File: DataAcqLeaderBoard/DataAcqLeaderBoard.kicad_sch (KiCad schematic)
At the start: 30 parts, among them SW1 UP, SW2 UP, SW3 UP, U1 PA1616S_GPS, X1 DigiXBeeRX900Micro

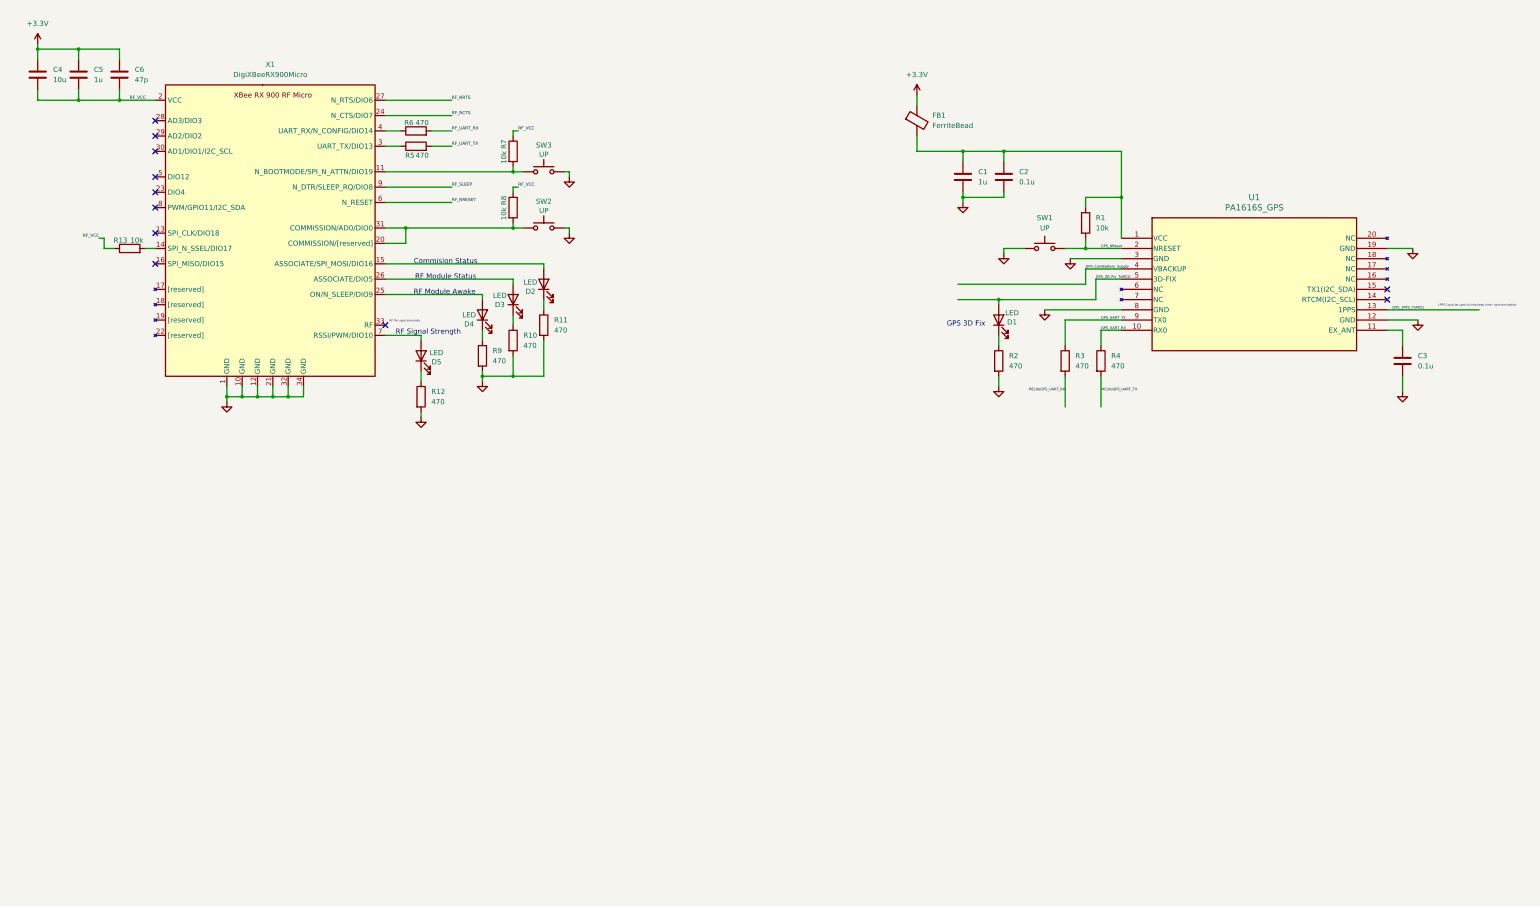
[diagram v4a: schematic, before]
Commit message: Added Digi XBee LTE Module
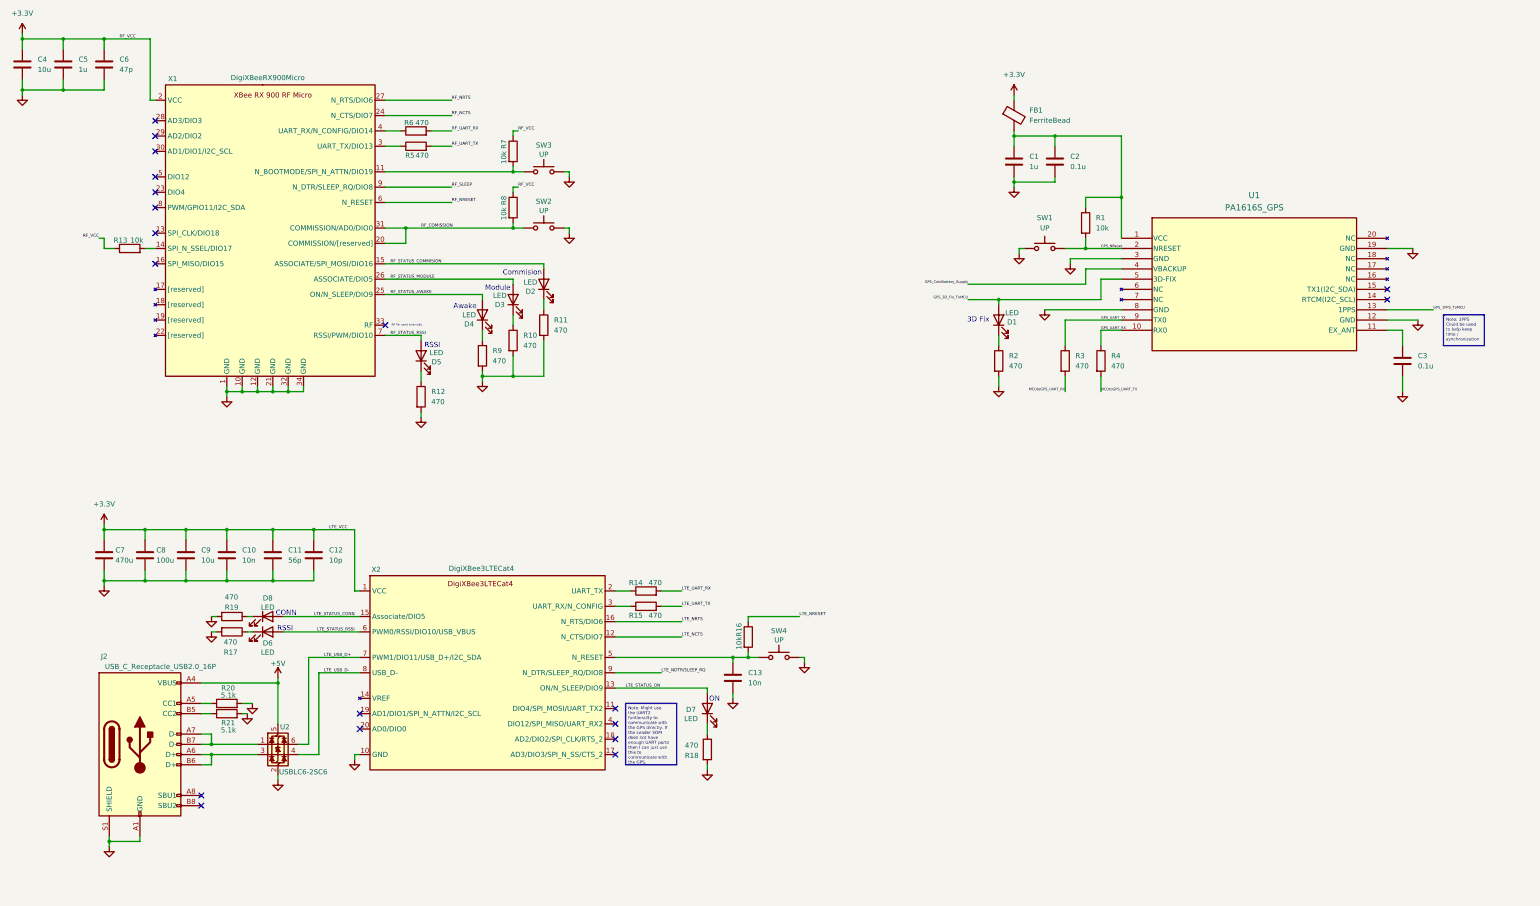
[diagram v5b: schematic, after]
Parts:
- added C10, C13: 10n, symbol Device:C
- added C11: 56p, symbol Device:C
- added C12: 10p, symbol Device:C
- added C7: 470u, symbol Device:C
- added C8: 100u, symbol Device:C
- added C9: 10u, symbol Device:C
- added D6, D7, D8: LED, symbol Device:LED
- added J2: USB_C_Receptacle_USB2.0_16P, symbol Connector:USB_C_Receptacle_USB2.0_16P
- added R14, R15, R17, R18, R19: 470, symbol Device:R
- added R16: 10k, symbol Device:R
- added R20, R21: 5.1k, symbol Device:R
- added SW4: UP, symbol Switch:SW_Push
- added U2: USBLC6-2SC6, Package_TO_SOT_SMD:SOT-23-6, symbol Power_Protection:USBLC6-2SC6
- added X2: DigiXBee3LTECat4, symbol DataAcqLeaderBoard-Symbols:DigiXBee3LTECat4
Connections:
- net +3.3V: now also R13.1, R7.1, R8.1, X1.2 (VCC), C10.1, C11.1, C12.1, C7.1, C8.1, C9.1, X2.1 (VCC)
- net GND: now also C4.2, C5.2, C6.2, C10.2, C11.2, C12.2, C13.2, C7.2, C8.2, C9.2, J2.A1 (GND), J2.A12 (GND), J2.B1 (GND), J2.B12 (GND), J2.S1 (SHIELD), R17.2, R18.2, R19.2, R20.2, R21.2, SW4.2, U2.2 (GND), X2.10 (GND)
- net RF_COMISSION: now reaches R8.2, SW2.1, X1.20 (COMMISSION/[reserved]), X1.31 (COMMISSION/AD0/DIO0)
- net RF_STATUS_MODULE: now reaches D3.2 (A), X1.26 (ASSOCIATE/DIO5)
- net RF_STATUS_COMMISION: now reaches D2.2 (A), X1.15 (ASSOCIATE/SPI_MOSI/DIO16)
- net RF_STATUS_AWAKE: now reaches D4.2 (A), X1.25 (ON/N_SLEEP/DIO9)
- net RF_STATUS_RSSI: now reaches D5.2 (A), X1.7 (RSSI/PWM/DIO10)
- removed net RF_VCC: C4.2, C5.2, C6.2, R13.1, R7.1, R8.1, X1.2 (VCC)
- new net: D7.1 (K), R18.1
- new net: R14.1, X2.2 (UART_TX)
- new net: C13.1, R16.2, SW4.1, X2.5 (N_RESET)
- new net: J2.A5 (CC1), R20.1
- new net: J2.A6 (D+), J2.B6 (D+), U2.3 (I/O2)
- new net: J2.A7 (D-), J2.B7 (D-), U2.1 (I/O1)
- new net: J2.B5 (CC2), R21.1
- new net: D6.1 (K), R17.1
- new net: D8.1 (K), R19.1
- new net: R15.1, X2.3 (UART_RX/N_CONFIG)
- new net +5V: J2.A4 (VBUS), J2.A9 (VBUS), J2.B4 (VBUS), J2.B9 (VBUS), U2.5 (VBUS)
- new net LTE_NCTS: X2.12 (N_CTS/DIO7)
- new net LTE_NDTR/SLEEP_RQ: X2.9 (N_DTR/SLEEP_RQ/DIO8)
- new net LTE_NRESET: R16.1
- new net LTE_NRTS: X2.16 (N_RTS/DIO6)
- new net LTE_STATUS_CONN: D8.2 (A), X2.15 (Associate/DIO5)
- new net LTE_STATUS_ON: D7.2 (A), X2.13 (ON/N_SLEEP/DIO9)
- new net LTE_STATUS_RSSI: D6.2 (A), X2.6 (PWM0/RSSI/DIO10/USB_VBUS)
- new net LTE_UART_RX: R14.2
- new net LTE_UART_TX: R15.2
- new net LTE_USB_D+: U2.6 (I/O1), X2.7 (PWM1/DIO11/USB_D+/I2C_SDA)
- new net LTE_USB_D-: U2.4 (I/O2), X2.8 (USB_D-)
- no-connect marks 11 -> 19
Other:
- note added: "3D Fix"
- note added: "Awake"
- note added: "CONN"
- note added: "Commision"
- note added: "Module"
- note added: "ON"
- note added: "RSSI"
- note removed: "1PPS Could be used to help keep time / synchronization"
- note removed: "Commision Status"
- note removed: "GPS 3D Fix"
- note removed: "RF Module Awake"
- note removed: "RF Module Status"
- note removed: "RF Signal Strength"
- moved on the sheet: C1, C2, C4, C5, C6, FB1

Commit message: Debounced Push Buttons
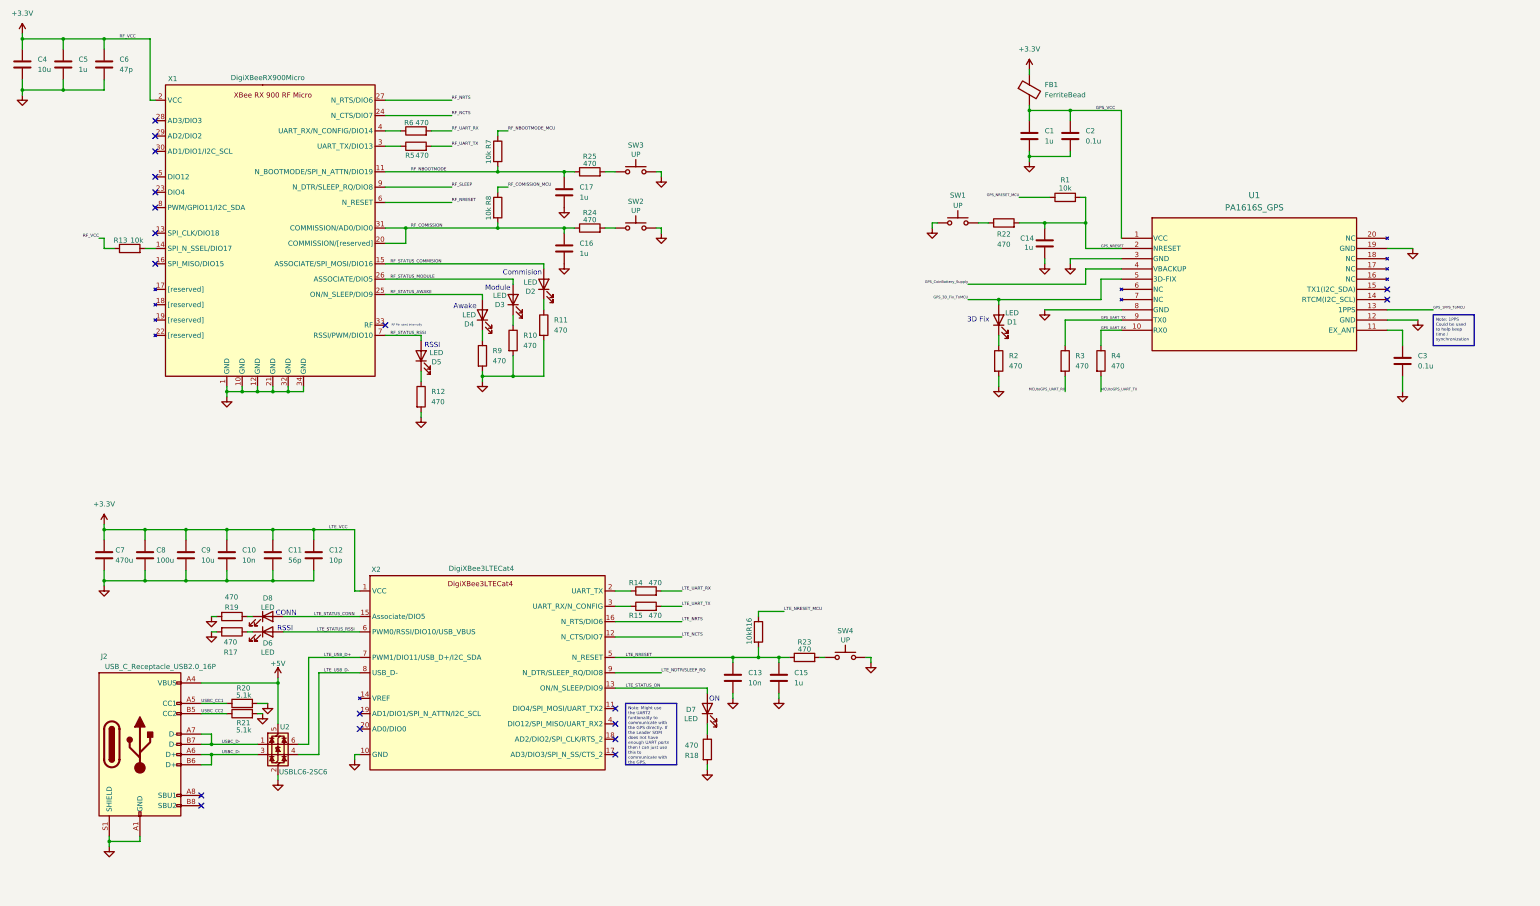
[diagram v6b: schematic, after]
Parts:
- added C14, C15, C16, C17: 1u, symbol Device:C
- added R22, R23, R24, R25: 470, symbol Device:R
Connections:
- net +3.3V: no longer R7.1, R8.1
- net GND: now also C14.2, C15.2, C16.2, C17.2
- net LTE_NRESET: now also C13.1, R16.2, X2.5 (N_RESET), C15.1, R23.1; no longer R16.1
- net RF_COMISSION: now also C16.1, R24.1; no longer SW2.1
- net GPS_VCC: now reaches C1.1, C2.1, FB1.2, U1.1 (VCC)
- net GPS_VCC: no longer R1.1
- net USBC_CC1: now reaches J2.A5 (CC1), R20.1
- net USBC_D-: now reaches J2.A6 (D+), J2.B6 (D+), U2.3 (I/O2)
- net USBC_D-: now also J2.A7 (D-), J2.B7 (D-), U2.1 (I/O1)
- net USBC_CC2: now reaches J2.B5 (CC2), R21.1
- net RF_NBOOTMODE: now reaches R7.2, X1.11 (N_BOOTMODE/SPI_N_ATTN/DIO19)
- net RF_NBOOTMODE: now also C17.1, R25.1; no longer SW3.1
- net GPS_NReset renamed GPS_NRESET
- net GPS_NRESET: now also C14.1, R22.2; no longer SW1.2
- new net: R25.2, SW3.1
- new net: R24.2, SW2.1
- new net: R23.2, SW4.1
- new net: R22.1, SW1.2
- new net GPS_NRESET_MCU: R1.1
- new net LTE_NRESET_MCU: R16.1
- new net RF_COMISSION_MCU: R8.1
- new net RF_NBOOTMODE_MCU: R7.1
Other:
- moved on the sheet: C1, C2, FB1, R1, R16, R20, R21, R8, SW1, SW2, SW4

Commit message: Added XBee RF and LTE Footprints
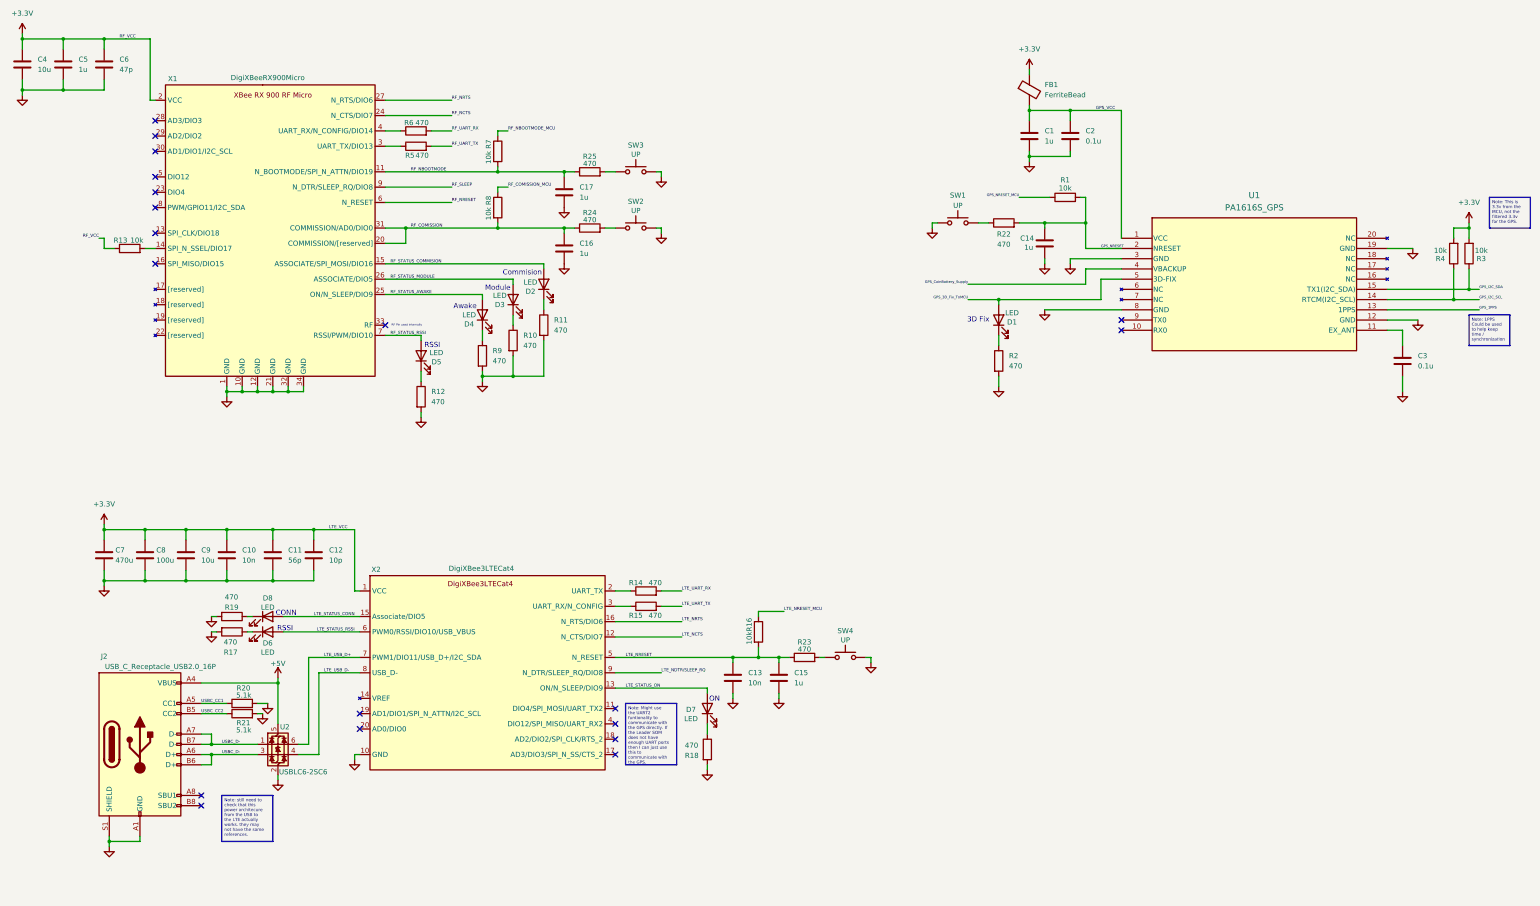
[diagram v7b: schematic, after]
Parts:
- R3, R4: value 470 -> 10k
- X1: footprint (none) -> DataAcqLeaderBoard-Footprints:XBeeXR900RFMicro
- X2: footprint (none) -> DataAcqLeaderBoard-Footprints:DigiXBee3LTECat4
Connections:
- net MCUtoGPS_UART_RX is gone; now on net +3.3V: R3.2
- net MCUtoGPS_UART_TX is gone; now on net +3.3V: R4.2
- net GPS_I2C_SCL: now reaches U1.14 (RTCM(I2C_SCL))
- net GPS_I2C_SCL: now also R4.1
- net GPS_I2C_SDA: now reaches U1.15 (TX1(I2C_SDA))
- net GPS_I2C_SDA: now also R3.1
- net GPS_1PPS_ToMCU renamed GPS_1PPS
- net GPS_UART_RX: no longer names the net of U1.10 (RX0)
- net GPS_UART_RX: no longer R4.1
- net GPS_UART_TX: no longer names the net of U1.9 (TX0)
- net GPS_UART_TX: no longer R3.1

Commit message: Interfaced Leader SOM and added UTSVT Library
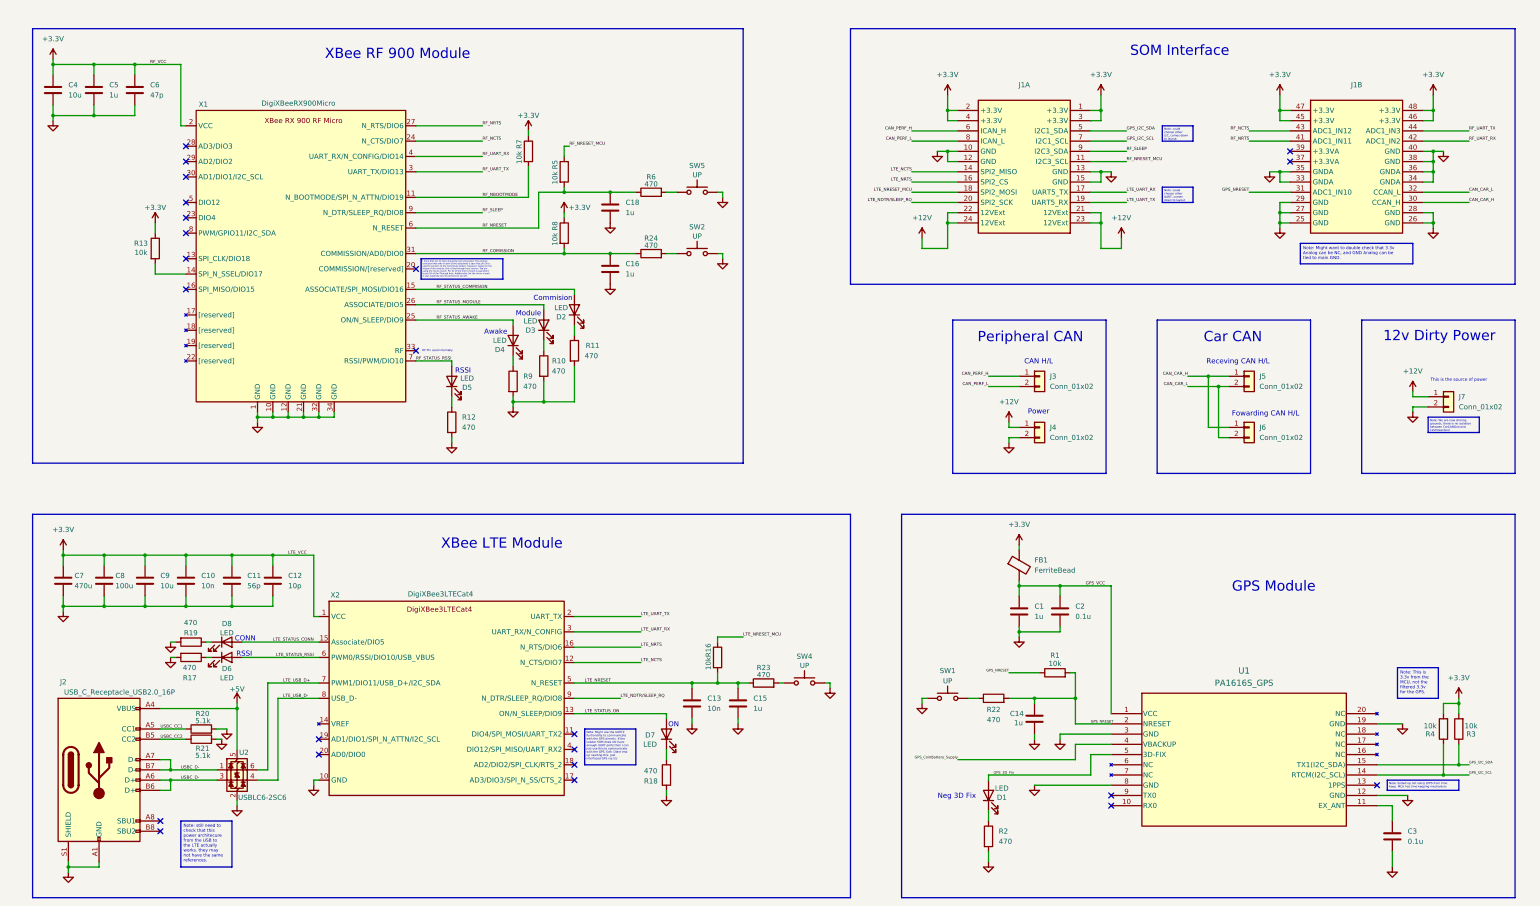
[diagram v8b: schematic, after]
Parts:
- removed C17: 1u, symbol Device:C
- removed R14, R15, R25: 470, symbol Device:R
- removed SW3: UP, symbol Switch:SW_Push
- added C18: 1u, symbol Device:C
- added J1: ~, UTSVT_Special:LeaderSOM, symbol utsvt-connector:LSOM_DaughterConn
- added J3, J4, J5, J6, J7: Conn_01x02, Connector_PinHeader_2.00mm:PinHeader_1x02_P2.00mm_Vertical, symbol Connector_Generic:Conn_01x02
- added SW5: UP, symbol Switch:SW_Push
- R5: value 470 -> 10k
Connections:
- net GPS_NRESET_MCU is gone; now on net GPS_NRESET: R1.1
- net RF_COMISSION_MCU is gone; now on net +3.3V: R8.1
- net RF_NBOOTMODE_MCU is gone; now on net +3.3V: R7.1
- net +3.3V: now also J1.1 (+3.3V), J1.2 (+3.3V), J1.3 (+3.3V), J1.4 (+3.3V), J1.45 (+3.3V), J1.46 (+3.3V), J1.47 (+3.3V), J1.48 (+3.3V)
- net GND: now also C18.2, J1.10 (GND), J1.12 (GND), J1.13 (GND), J1.15 (GND), J1.25 (GND), J1.26 (GND), J1.27 (GND), J1.28 (GND), J1.29 (GND), J1.33 (GNDA), J1.34 (GNDA), J1.35 (GNDA), J1.36 (GNDA), J1.38 (GND), J1.40 (GND), J4.2 (Pin_2), J7.2 (Pin_2), SW5.2
- net GPS_I2C_SCL: now also J1.7 (I2C1_SCL)
- net GPS_I2C_SDA: now also J1.5 (I2C1_SDA)
- net GPS_NRESET: now also J1.31 (ADC1_IN10)
- net LTE_NCTS: now also J1.14 (SPI2_MISO)
- net LTE_NDTR/SLEEP_RQ: now also J1.20 (SPI2_SCK)
- net LTE_NRESET_MCU: now also J1.18 (SPI2_MOSI)
- net LTE_NRTS: now also J1.16 (SPI2_CS)
- net LTE_UART_RX: now also X2.3 (UART_RX/N_CONFIG), J1.17 (UART5_TX)
- net LTE_UART_TX: now also X2.2 (UART_TX), J1.19 (UART5_RX)
- net RF_COMISSION: no longer X1.20 (COMMISSION/[reserved])
- net RF_NCTS: now also J1.43 (ADC1_IN12)
- net RF_NRESET: now also R5.2, R6.1, C18.1
- net RF_NRTS: now also J1.41 (ADC1_IN11)
- net RF_SLEEP: now also J1.9 (I2C3_SDA)
- net RF_UART_RX: now also X1.4 (UART_RX/N_CONFIG/DIO14), J1.42 (ADC1_IN2); no longer R6.2
- net RF_UART_TX: now also X1.3 (UART_TX/DIO13), J1.44 (ADC1_IN3); no longer R5.2
- net RF_NRESET_MCU: now reaches R5.1
- net RF_NRESET_MCU: now also J1.11 (I2C3_SCL); no longer X1.3 (UART_TX/DIO13)
- net GPS_1PPS: no longer names the net of U1.13 (1PPS)
- net GPS_3D_Fix_ToMCU renamed GPS_3D_Fix
- new net: R6.2, SW5.1
- new net +12V: J1.21 (12VExt), J1.22 (12VExt), J1.23 (12VExt), J1.24 (12VExt), J4.1 (Pin_1), J7.1 (Pin_1)
- new net CAN_CAR_H: J1.30 (CCAN_H), J5.1 (Pin_1), J6.1 (Pin_1)
- new net CAN_CAR_L: J1.32 (CCAN_L), J5.2 (Pin_2), J6.2 (Pin_2)
- new net CAN_PERF_H: J1.6 (ICAN_H), J3.1 (Pin_1)
- new net CAN_PERF_L: J1.8 (ICAN_L), J3.2 (Pin_2)
- no-connect marks 19 -> 23
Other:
- note added: "12v Dirty Power"
- note added: "CAN H/L"
- note added: "Car CAN"
- note added: "Fowarding CAN H/L"
- note added: "GPS Module"
- note added: "Neg 3D Fix"
- note added: "Peripheral CAN"
- note added: "Power"
- note added: "Receving CAN H/L"
- note added: "SOM Interface"
- note added: "This is the source of power"
- note added: "XBee LTE Module"
- note added: "XBee RF 900 Module"
- note removed: "3D Fix"
- moved on the sheet: C1, C10, C11, C12, C13, C14, C15, C16, C2, C3, C4, C5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
